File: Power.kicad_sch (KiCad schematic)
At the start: 46 parts, among them J14 Conn_01x06, Q2 MBT2222ADW1T1, Q3 MBT2222ADW1T1, U17 BQ25883RGER, U21 TPS7A4501DCQT, U4 ADM1176-1ARMZ-R7, U5 TPS54226PWPR

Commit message: Complete layout
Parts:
- removed R8: ?, Resistor_SMD:R_2512_6332Metric, symbol mainboard:R-US_R2512
- added R8: ?R, Resistor_SMD:R_2512_6332Metric, symbol Device:R_Small
- C18: renamed from C19; footprint Capacitor_SMD:C_1210_3225Metric -> Capacitor_SMD:C_0805_2012Metric
- C19: renamed from C20; footprint Capacitor_SMD:C_1210_3225Metric -> Capacitor_SMD:C_0805_2012Metric
- L2: footprint mainboard:L_2141 -> Inductor_SMD:L_1812_4532Metric
- L3: renamed from L4; footprint mainboard:L_2510 -> Inductor_SMD:L_Wuerth_MAPI-2510
- U6: renamed from U21; footprint (none) -> Package_TO_SOT_SMD:SOT-223-6; symbol mainboard:TPS7A4501DCQT -> Mainboard:TPS7A4501DCQT
- U7: renamed from U5; footprint (none) -> Package_SO:HTSSOP-14-1EP_4.4x5mm_P0.65mm_EP3.4x5mm_Mask3x3.1mm; symbol mainboard:TPS54226PWPRPWP14_2P31X2P46-L -> Mainboard:TPS54226PWPR
- U8: renamed from U17; footprint mainboard:QFN50P400X400X100-25N-D -> Package_DFN_QFN:Texas_RGE0024H_VQFN-24-1EP_4x4mm_P0.5mm_EP2.7x2.7mm; symbol mainboard:BQ25883RGER -> Mainboard:BQ25883RGER
- U9: renamed from U4; footprint (none) -> Package_SO:MSOP-10_3x3mm_P0.5mm; symbol mainboard:ADM1176-1ARMZ-R7 -> Mainboard:ADM1176-1ARMZ-R7
- renumbered C21 to C20, C18 to C21, C17 to C22, C26 to C23, C27 to C24, C6 to C25, C47 to C48, C43 to C49, C32 to C50, D5 to D3, J14 to J21, R110 to R77
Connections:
- net VBATT: now also J21.2 (Pin_2), R8.2
- net VSYS: now also R8.1; no longer J21.2 (Pin_2)
- net +3.3V renamed 3.3V
- net RF_EN renamed UHF_EN
- net SCL_PWR renamed PWR_SCL
- net SDA_PWR renamed PWR_SDA
- net USB_D+ renamed USB_D1+
- net USB_D- renamed USB_D1-
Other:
- note added: "Board Power Monitor"
- note removed: "Battery Power Monitor"
- moved on the sheet: R26

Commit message: v1 Final
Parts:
- R59: value 2.5K -> 3.16K
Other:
- note added: "Set RF Voltage: VOUT=1.21*(1+R55/R59)+(3E-6*R55) VOUT=5.07V (R55=10K, R59=3.16K)"
- note removed: "Set RF Voltage: VOUT=1.21*(1+R55/R59)+(3E-6*R55) VOUT=6.08V (R55=10K, R59=2.5K)"
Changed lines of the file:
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@@
 		)
 	)
-	(text "Set RF Voltage:\nVOUT=1.21*(1+R55/R59)+(3E-6*R55)\nVOUT=6.08V (R55=10K, R59=2.5K)\n"
+	(text "Set RF Voltage:\nVOUT=1.21*(1+R55/R59)+(3E-6*R55)\nVOUT=5.07V (R55=10K, R59=3.16K)\n"
 		(exclude_from_sim no)
 		(at 117.602 57.15 0)
@@
 			)
 		)
-		(property "Value" "2.5K"
+		(property "Value" "3.16K"
 			(at 109.474 55.626 0)
 			(effects

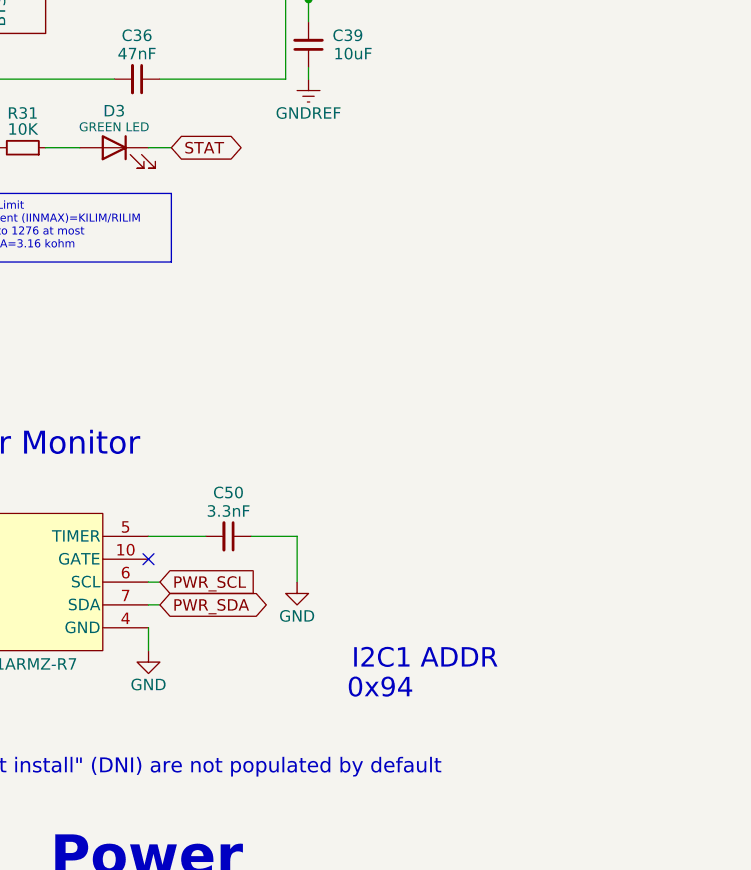
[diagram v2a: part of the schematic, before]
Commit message: Fixed/Added I2C addresses to schematic
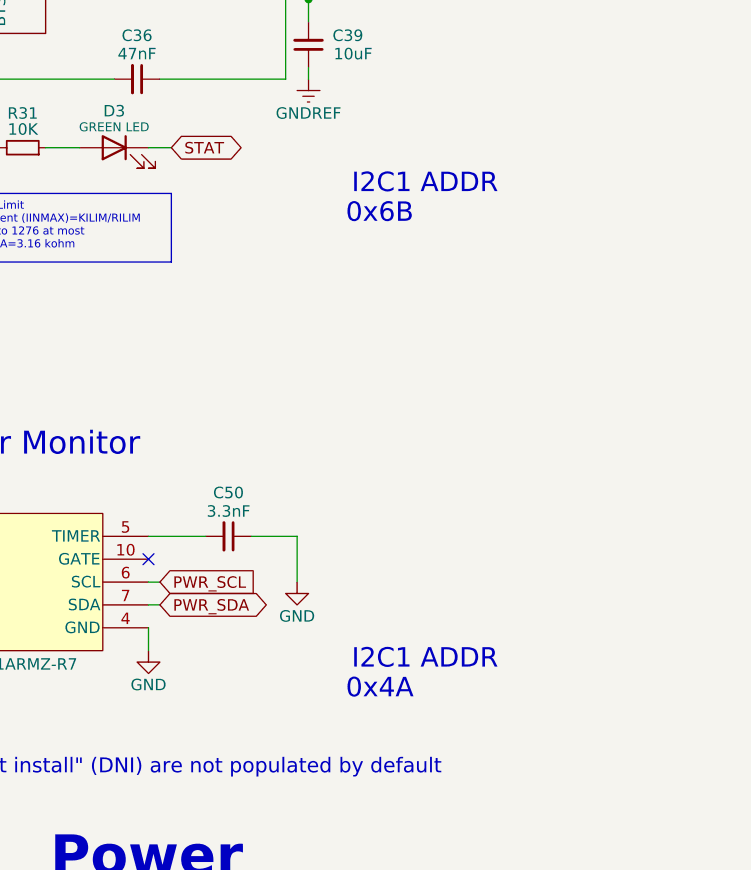
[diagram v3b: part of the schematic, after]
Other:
- note added: "0x4A"
- note added: "0x6B"
- note removed: "0x94"
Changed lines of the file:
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@@
+		)
+	)
+	(text "0x6B"
+		(exclude_from_sim no)
+		(at 263.144 103.886 0)
+		(effects
+			(font
+				(size 2.159 2.159)
+			)
+			(justify right bottom)
 		)
 	)
@@
 		)
 	)
+	(text "I2C1 ADDR"
+		(exclude_from_sim no)
+		(at 272.542 100.584 0)
+		(effects
+			(font
+				(size 2.159 2.159)
+			)
+			(justify right bottom)
+		)
+	)
 	(text "Power"
 		(exclude_from_sim no)
@@
 		)
 	)
-	(text "0x94"
+	(text "0x4A"
 		(exclude_from_sim no)
 		(at 263.144 156.718 0)

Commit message: v1.1 Schematic
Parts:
- removed C50: 3.3nF, Capacitor_SMD:C_0603_1608Metric, symbol Device:C_Small
- removed R26: 1K, Resistor_SMD:R_0603_1608Metric, symbol Device:R_Small
- removed R8: ?R, Resistor_SMD:R_2512_6332Metric, symbol Device:R_Small
- removed U9: ADM1176-1ARMZ-R7, Package_SO:MSOP-10_3x3mm_P0.5mm, symbol Mainboard:ADM1176-1ARMZ-R7
- added Q18, Q22: IRLML2803, Package_TO_SOT_SMD:SOT-23, symbol Mainboard:IRLML2803
- added Q19, Q23: IRF7404, Package_SO:SOIC-8_3.9x4.9mm_P1.27mm, symbol Mainboard:IRF7404
- added R11, R12: 10K, Resistor_SMD:R_0603_1608Metric, symbol Device:R_Small
- added R16, R17: 4.7K, Resistor_SMD:R_0603_1608Metric, symbol Device:R_Small
- added R18, R19: 3.3K, Resistor_SMD:R_0603_1608Metric, symbol Device:R_Small
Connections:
- net 3.3V: now also Q19.1 (Source), Q19.2 (Source), Q19.3 (Source), Q23.1 (Source), Q23.2 (Source), Q23.3 (Source), R18.1, R19.1
- net GND: now also Q18.2 (S), Q22.2 (S), R11.2, R12.2
- net UHF_EN: now also R11.1, R16.1
- new net: Q18.1 (G), R16.2
- new net: Q18.3 (D), Q19.4 (Gate), R18.2
- new net: Q22.1 (G), R17.2
- new net: Q22.3 (D), Q23.4 (Gate), R19.2
- new net GPS_EN: R12.1, R17.1
- new net GPS_VDD: Q23.5 (Drain), Q23.6 (Drain), Q23.7 (Drain), Q23.8 (Drain)
- new net RF_3.3V: Q19.5 (Drain), Q19.6 (Drain), Q19.7 (Drain), Q19.8 (Drain)
- no-connect marks 7 -> 4
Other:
- note added: "GPS Power"
- note added: "UHF 3.3V"
- note removed: "0x4A"
- note removed: "Board Power Monitor"
- moved on the sheet: C18, C19, C20, C21, C22, C23, C24, C25, C33, C34, C35, C36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
